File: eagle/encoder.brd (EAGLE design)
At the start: 100 x 80 mm, 22 parts, among them IC1 LM339D, J1 SPI, U1 MCP42XXX, U2 ATMEGA328P

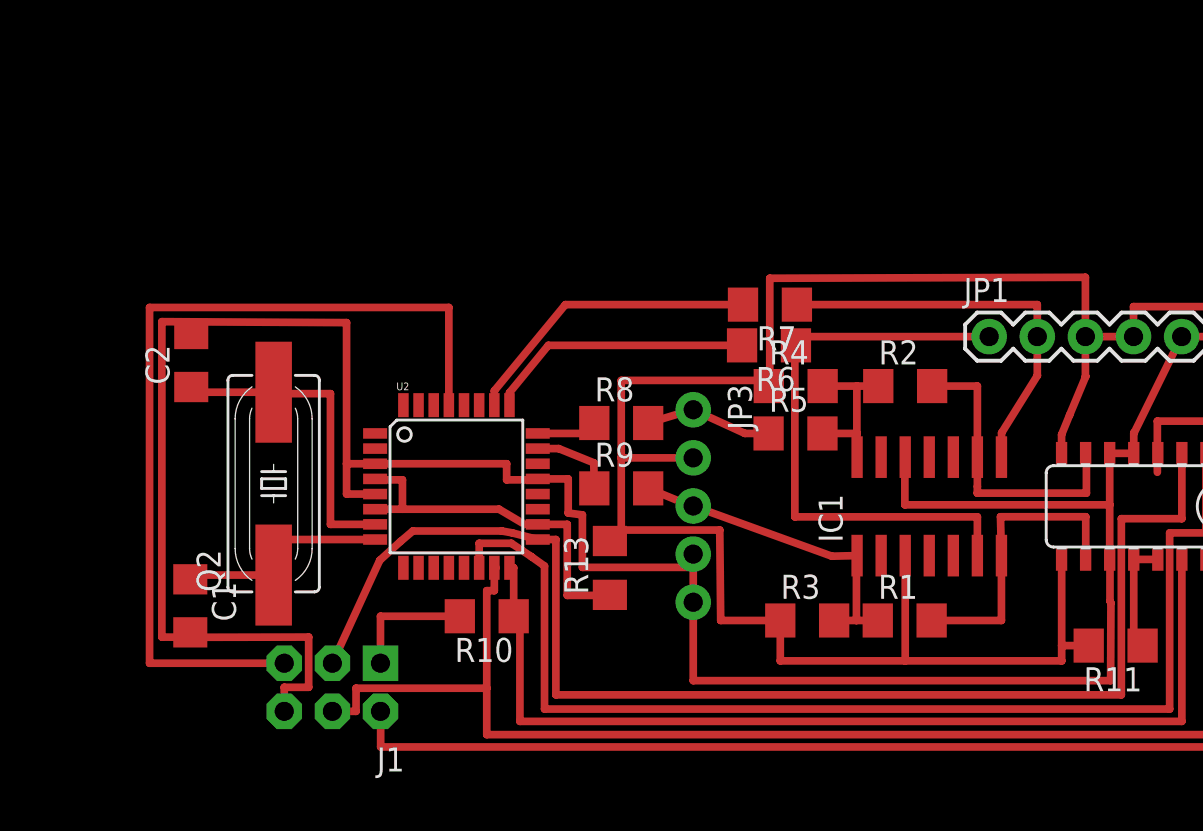
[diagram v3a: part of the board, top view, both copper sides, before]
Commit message: Added I2C and power connections.
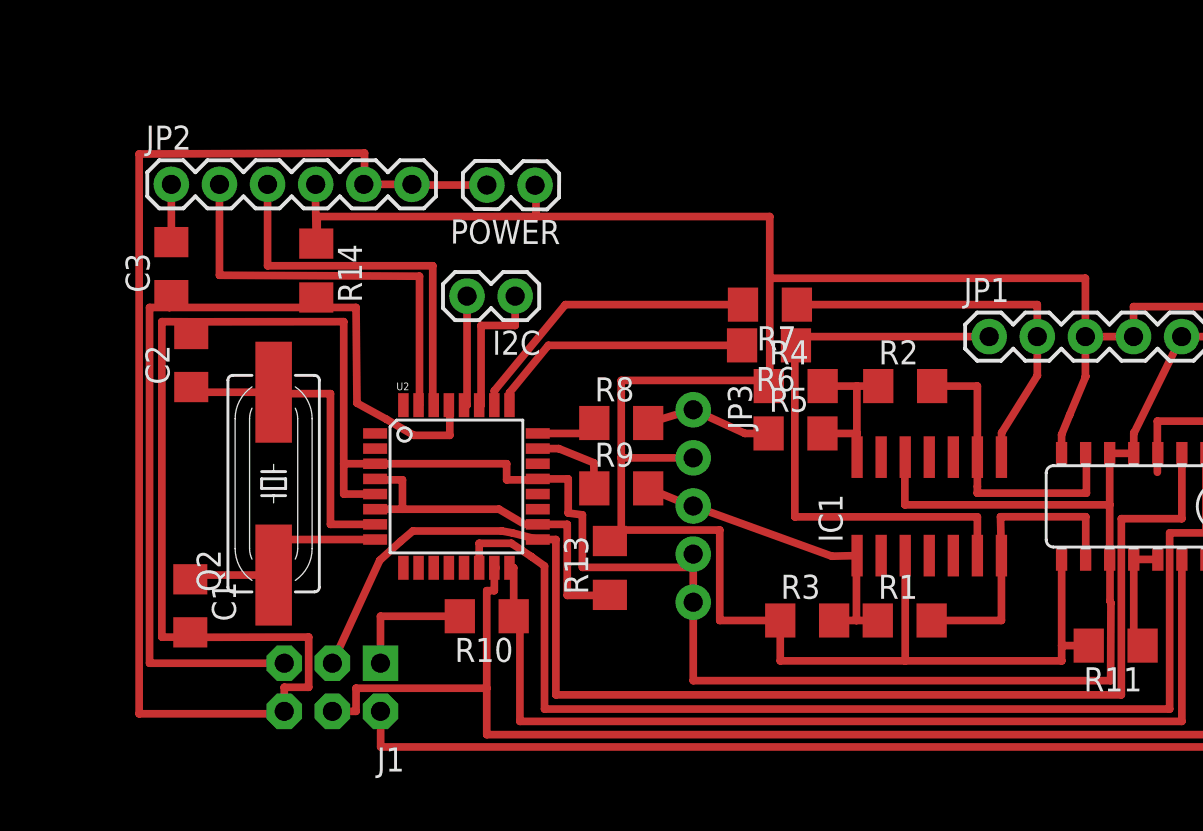
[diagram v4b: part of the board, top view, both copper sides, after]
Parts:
- added C3: 10uf, resistor:C1206
- added I2C, POWER: M02PTH, SparkFun-Connectors:1X02
- added JP2: Serial, SparkFun-Connectors:1X06
- added R14: 10k, resistor:R1206
- C1, C2: value (none) -> 22pf
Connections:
- new net DTR: C3.2, JP2.1
- new net N$12: I2C.1, U2.27
- new net N$13: I2C.2, U2.28
- new net RX-I: JP2.3, U2.30
- new net TX-O: JP2.2, U2.31
- net +5V: now also JP2.4, POWER.1, R14.1
- net GND: now also JP2.5, JP2.6, POWER.2
- net RESET: now also C3.1, R14.2
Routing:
- net GND: track 139.5 -> 197.1 mm
- net +5V: track 182.7 -> 216.2 mm
- net TX-O: track 0.00 -> 22.2 mm
- net RX-I: track 0.00 -> 20.4 mm
- net N$12: track 0.00 -> 7.66 mm
- net N$13: track 0.00 -> 5.92 mm
- net RESET: track 46.8 -> 50.2 mm
- net DTR: track 0.00 -> 3.05 mm
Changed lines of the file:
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@@
 <attribute name="OC_FARNELL" value="unknown" x="41.95" y="50.4" size="1.778" layer="27" rot="R90" display="off"/>
 </element>
-<element name="C1" library="resistor" package="C1206" value="" x="37.55" y="43.95" rot="R270"/>
-<element name="C2" library="resistor" package="C1206" value="" x="37.6" y="56.9" rot="R90"/>
+<element name="C1" library="resistor" package="C1206" value="22pf" x="37.55" y="43.95" rot="R270"/>
+<element name="C2" library="resistor" package="C1206" value="22pf" x="37.6" y="56.9" rot="R90"/>
+<element name="R14" library="resistor" package="R1206" value="10k" x="44.2" y="61.65" rot="R270"/>
+<element name="C3" library="resistor" package="C1206" value="10uf" x="36.55" y="61.75" rot="R90"/>
+<element name="JP2" library="SparkFun-Connectors" package="1X06" value="Serial" x="36.55" y="66.2"/>
+<element name="I2C" library="SparkFun-Connectors" package="1X02" value="M02PTH" x="54.7" y="60.3" rot="R180"/>
+<element name="POWER" library="SparkFun-Connectors" package="1X02" value="M02PTH" x="55.75" y="66.15" rot="R179.7"/>
 </elements>
 <signals>
@@
 <contactref element="U2" pad="3"/>
 <contactref element="U2" pad="5"/>
-<wire x1="47.3074" y1="49.85" x2="45.8" y2="49.85" width="0.4064" layer="1"/>
+<wire x1="47.3074" y1="49.85" x2="45.65" y2="49.85" width="0.4064" layer="1"/>
 <wire x1="43.8" y1="39.65" x2="42.51" y2="39.65" width="0.4064" layer="1"/>
 <wire x1="42.51" y1="39.65" x2="42.51" y2="38.38" width="0.4064" layer="1"/>
-<wire x1="47.3074" y1="51.45" x2="45.8" y2="51.45" width="0.4064" layer="1"/>
-<wire x1="45.8" y1="51.45" x2="45.8" y2="49.85" width="0.4064" layer="1"/>
+<wire x1="47.3074" y1="51.45" x2="45.65" y2="51.45" width="0.4064" layer="1"/>
+<wire x1="45.65" y1="51.45" x2="45.65" y2="49.85" width="0.4064" layer="1"/>
 <wire x1="47.3074" y1="51.45" x2="54.25" y2="51.45" width="0.4064" layer="1"/>
 <wire x1="54.25" y1="51.45" x2="54.25" y2="50.6" width="0.4064" layer="1"/>
@@
 <contactref element="C1" pad="2"/>
 <contactref element="C2" pad="2"/>
-<wire x1="45.8" y1="51.45" x2="45.8" y2="58.9" width="0.4064" layer="1"/>
-<wire x1="45.8" y1="58.9" x2="37.653034375" y2="58.941778125" width="0.4064" layer="1"/>
+<wire x1="45.65" y1="51.45" x2="45.65" y2="58.95" width="0.4064" layer="1"/>
+<wire x1="45.65" y1="58.95" x2="37.653034375" y2="58.941778125" width="0.4064" layer="1"/>
 <wire x1="37.653034375" y1="58.941778125" x2="36.05" y2="58.95" width="0.4064" layer="1"/>
 <wire x1="36.05" y1="58.95" x2="36.05" y2="42.3" width="0.4064" layer="1"/>
@@
 <wire x1="37.55" y1="42.55" x2="37.6989625" y2="42.55" width="0.4064" layer="1"/>
 <wire x1="37.6989625" y1="42.55" x2="37.6989625" y2="42.2893625" width="0.4064" layer="1"/>
+<contactref element="JP2" pad="5"/>
+<contactref element="JP2" pad="6"/>
+<wire x1="46.71" y1="66.2" x2="46.75" y2="66.2" width="0.4064" layer="1"/>
+<wire x1="46.75" y1="66.2" x2="46.75" y2="67.85" width="0.4064" layer="1"/>
+<wire x1="46.75" y1="67.85" x2="34.85" y2="67.8" width="0.4064" layer="1"/>
+<wire x1="34.85" y1="67.8" x2="34.85" y2="38.25" width="0.4064" layer="1"/>
+<wire x1="34.85" y1="38.25" x2="42.51" y2="38.25" width="0.4064" layer="1"/>
+<wire x1="42.51" y1="38.25" x2="42.51" y2="38.38" width="0.4064" layer="1"/>
+<wire x1="46.75" y1="66.2" x2="49.25" y2="66.2" width="0.4064" layer="1"/>
+<contactref element="POWER" pad="2"/>
+<wire x1="53.210034375" y1="66.163296875" x2="49.25" y2="66.163296875" width="0.4064" layer="1"/>
+<wire x1="49.25" y1="66.163296875" x2="49.25" y2="66.2" width="0.4064" layer="1"/>
 </signal>
 <signal name="N$5">
@@
 <wire x1="68.088" y1="55.55" x2="68.140275" y2="55.55" width="0.4064" layer="1"/>
 <wire x1="68.140275" y1="55.55" x2="68.140275" y2="61.242184375" width="0.4064" layer="1"/>
-<wire x1="68.140275" y1="61.242184375" x2="84.8028875" y2="61.292184375" width="0.4064" layer="1"/>
-<wire x1="84.8028875" y1="61.292184375" x2="84.8028875" y2="58.1605125" width="0.4064" layer="1"/>
+<wire x1="68.140275" y1="61.242184375" x2="84.8028875" y2="61.242184375" width="0.4064" layer="1"/>
+<wire x1="84.8028875" y1="61.242184375" x2="84.8028875" y2="58.1605125" width="0.4064" layer="1"/>
 <wire x1="68.69481875" y1="43.176359375" x2="68.97244375" y2="43.176359375" width="0.4064" layer="1"/>
 <wire x1="68.69481875" y1="41.044434375" x2="75.29" y2="41.044434375" width="0.4064" layer="1"/>
@@
 <wire x1="60.3" y1="55.85" x2="68.088" y2="55.85" width="0.4064" layer="1"/>
 <wire x1="68.088" y1="55.85" x2="68.088" y2="55.55" width="0.4064" layer="1"/>
-<wire x1="68.69481875" y1="43.176359375" x2="65.55" y2="43.176359375" width="0.4064" layer="1"/>
-<wire x1="65.55" y1="43.176359375" x2="65.5" y2="47.95" width="0.4064" layer="1"/>
+<wire x1="68.69481875" y1="43.176359375" x2="65.5" y2="43.176359375" width="0.4064" layer="1"/>
+<wire x1="65.5" y1="43.176359375" x2="65.5" y2="47.95" width="0.4064" layer="1"/>
 <wire x1="65.5" y1="47.95" x2="60.3" y2="47.95" width="0.4064" layer="1"/>
 <wire x1="68.69481875" y1="41.044434375" x2="68.69481875" y2="43.176359375" width="0.4064" layer="1"/>
@@
 <wire x1="59.7" y1="47.372" x2="60.3" y2="47.372" width="0.4064" layer="1"/>
 <wire x1="60.3" y1="47.372" x2="60.3" y2="47.95" width="0.4064" layer="1"/>
+<contactref element="R14" pad="1"/>
+<contactref element="JP2" pad="4"/>
+<wire x1="44.25" y1="64.5" x2="55.8" y2="64.5" width="0.4064" layer="1"/>
+<wire x1="55.8" y1="64.5" x2="68.140275" y2="64.5" width="0.4064" layer="1"/>
+<wire x1="68.140275" y1="64.5" x2="68.140275" y2="61.242184375" width="0.4064" layer="1"/>
+<wire x1="44.17" y1="66.2" x2="44.15" y2="66.05" width="0.4064" layer="1"/>
+<wire x1="44.15" y1="66.05" x2="44.2" y2="63.072" width="0.4064" layer="1"/>
+<wire x1="44.2" y1="63.072" x2="44.25" y2="63.072" width="0.4064" layer="1"/>
+<wire x1="44.25" y1="63.072" x2="44.25" y2="64.5" width="0.4064" layer="1"/>
+<contactref element="POWER" pad="1"/>
+<wire x1="55.75" y1="66.15" x2="55.8" y2="66.15" width="0.4064" layer="1"/>
+<wire x1="55.8" y1="66.15" x2="55.8" y2="64.5" width="0.4064" layer="1"/>
 </signal>
 <signal name="B-REF">
@@
 <signal name="RESET">
 <contactref element="U2" pad="29"/>
-<wire x1="51.2" y1="54.5426" x2="51.2" y2="59.7" width="0.4064" layer="1"/>
+<wire x1="51.2" y1="54.5426" x2="51.25" y2="54.5426" width="0.4064" layer="1"/>
+<wire x1="51.25" y1="54.5426" x2="51.25" y2="52.95" width="0.4064" layer="1"/>
+<wire x1="51.25" y1="52.95" x2="49.35" y2="52.95" width="0.4064" layer="1"/>
+<wire x1="49.35" y1="52.95" x2="47.9" y2="53.8" width="0.4064" layer="1"/>
+<wire x1="47.9" y1="53.8" x2="46.35" y2="54.65" width="0.4064" layer="1"/>
+<wire x1="46.35" y1="54.65" x2="46.3" y2="59.7" width="0.4064" layer="1"/>
 <contactref element="J1" pad="5"/>
 <wire x1="42.51" y1="40.92" x2="35.4" y2="40.92" width="0.4064" layer="1"/>
 <wire x1="35.4" y1="40.92" x2="35.4" y2="59.7" width="0.4064" layer="1"/>
-<wire x1="35.4" y1="59.7" x2="51.2" y2="59.7" width="0.4064" layer="1"/>
+<wire x1="35.4" y1="59.7" x2="36.45" y2="59.7" width="0.4064" layer="1"/>
+<contactref element="R14" pad="2"/>
+<contactref element="C3" pad="1"/>
+<wire x1="36.45" y1="59.7" x2="44.3" y2="59.7" width="0.4064" layer="1"/>
+<wire x1="44.3" y1="59.7" x2="46.3" y2="59.7" width="0.4064" layer="1"/>
+<wire x1="36.55" y1="60.35" x2="36.45" y2="60.35" width="0.4064" layer="1"/>
+<wire x1="36.45" y1="60.35" x2="36.45" y2="59.7" width="0.4064" layer="1"/>
+<wire x1="44.2" y1="60.228" x2="44.3" y2="60.228" width="0.4064" layer="1"/>
+<wire x1="44.3" y1="60.228" x2="44.3" y2="59.7" width="0.4064" layer="1"/>
 </signal>
 <signal name="SS">
@@
 <wire x1="37.6" y1="55.226" x2="37.6" y2="55.5" width="0.4064" layer="1"/>
 </signal>
+<signal name="DTR">
+<contactref element="C3" pad="2"/>
+<contactref element="JP2" pad="1"/>
+<wire x1="36.55" y1="66.2" x2="36.55" y2="63.15" width="0.4064" layer="1"/>
+</signal>
+<signal name="TX-O">
+<contactref element="U2" pad="31"/>
+<contactref element="JP2" pad="2"/>
+<wire x1="49.6" y1="54.5426" x2="49.65" y2="54.5426" width="0.4064" layer="1"/>
+<wire x1="49.65" y1="54.5426" x2="49.65" y2="61.35" width="0.4064" layer="1"/>
+<wire x1="49.65" y1="61.35" x2="39.09" y2="61.4" width="0.4064" layer="1"/>
+<wire x1="39.09" y1="61.4" x2="39.09" y2="66.2" width="0.4064" layer="1"/>
+</signal>
+<signal name="RX-I">
+<contactref element="U2" pad="30"/>
+<contactref element="JP2" pad="3"/>
+<wire x1="50.4" y1="54.5426" x2="50.35" y2="54.5426" width="0.4064" layer="1"/>
+<wire x1="50.35" y1="54.5426" x2="50.35" y2="61.9" width="0.4064" layer="1"/>
+<wire x1="50.35" y1="61.9" x2="41.63" y2="61.9" width="0.4064" layer="1"/>
+<wire x1="41.63" y1="61.9" x2="41.63" y2="66.2" width="0.4064" layer="1"/>
+</signal>
+<signal name="N$12">
+<contactref element="U2" pad="27"/>
+<contactref element="I2C" pad="1"/>
+<wire x1="52.8" y1="54.5426" x2="52.9" y2="54.5426" width="0.4064" layer="1"/>
+<wire x1="52.9" y1="54.5426" x2="52.9" y2="58.75" width="0.4064" layer="1"/>
+<wire x1="52.9" y1="58.75" x2="54.7" y2="58.75" width="0.4064" layer="1"/>
+<wire x1="54.7" y1="58.75" x2="54.7" y2="60.3" width="0.4064" layer="1"/>
+</signal>
+<signal name="N$13">
+<contactref element="U2" pad="28"/>
+<contactref element="I2C" pad="2"/>
+<wire x1="52" y1="54.5426" x2="52.16" y2="54.5426" width="0.4064" layer="1"/>
+<wire x1="52.16" y1="54.5426" x2="52.16" y2="60.3" width="0.4064" layer="1"/>
+</signal>
 </signals>

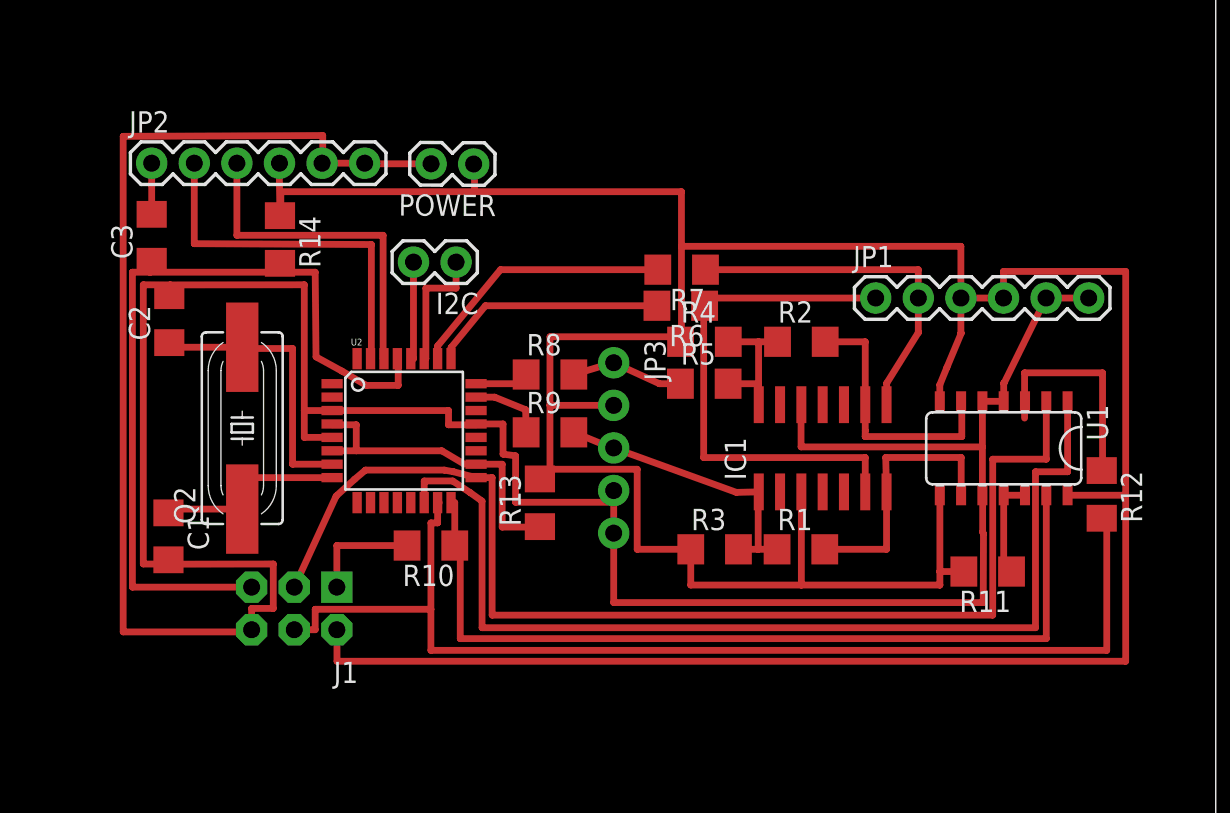
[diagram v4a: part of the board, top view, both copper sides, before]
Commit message: Moved components closer together
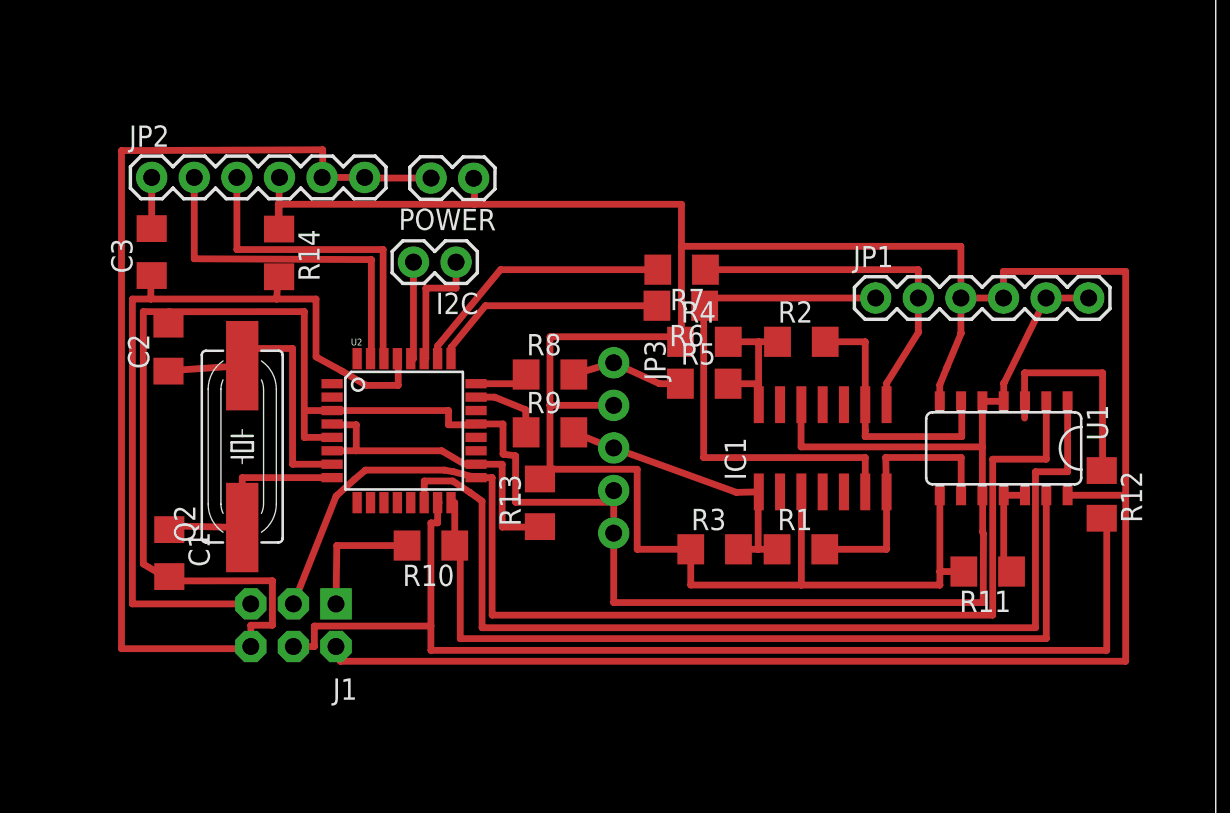
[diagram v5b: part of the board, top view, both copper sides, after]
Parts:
- moved C2 1.70 mm to (37.5, 55.2)
- moved Q2 1.10 mm to (42.0, 49.3)
- moved C1 1.00 mm to (37.6, 43.0)
- moved J1 1.00 mm to (45.0, 38.6)
- moved JP2 0.85 mm to (36.5, 65.3)
- moved POWER 0.85 mm to (55.8, 65.3)
- moved C3 0.85 mm to (36.5, 60.9)
- moved R14 0.80 mm to (44.1, 60.9)
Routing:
- net GND: track 197.1 -> 194.5 mm
- net +5V: track 216.2 -> 214.3 mm
- net N$10: track 11.9 -> 12.9 mm
- net N$2: track 6.67 -> 7.67 mm
- net SCK: track 69.9 -> 70.9 mm
- net TX-O: track 22.2 -> 21.4 mm
- net RX-I: track 20.4 -> 19.6 mm
- net N$11: track 17.0 -> 17.7 mm
- net RESET: track 50.2 -> 49.5 mm
